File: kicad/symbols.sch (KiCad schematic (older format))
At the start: 13 parts

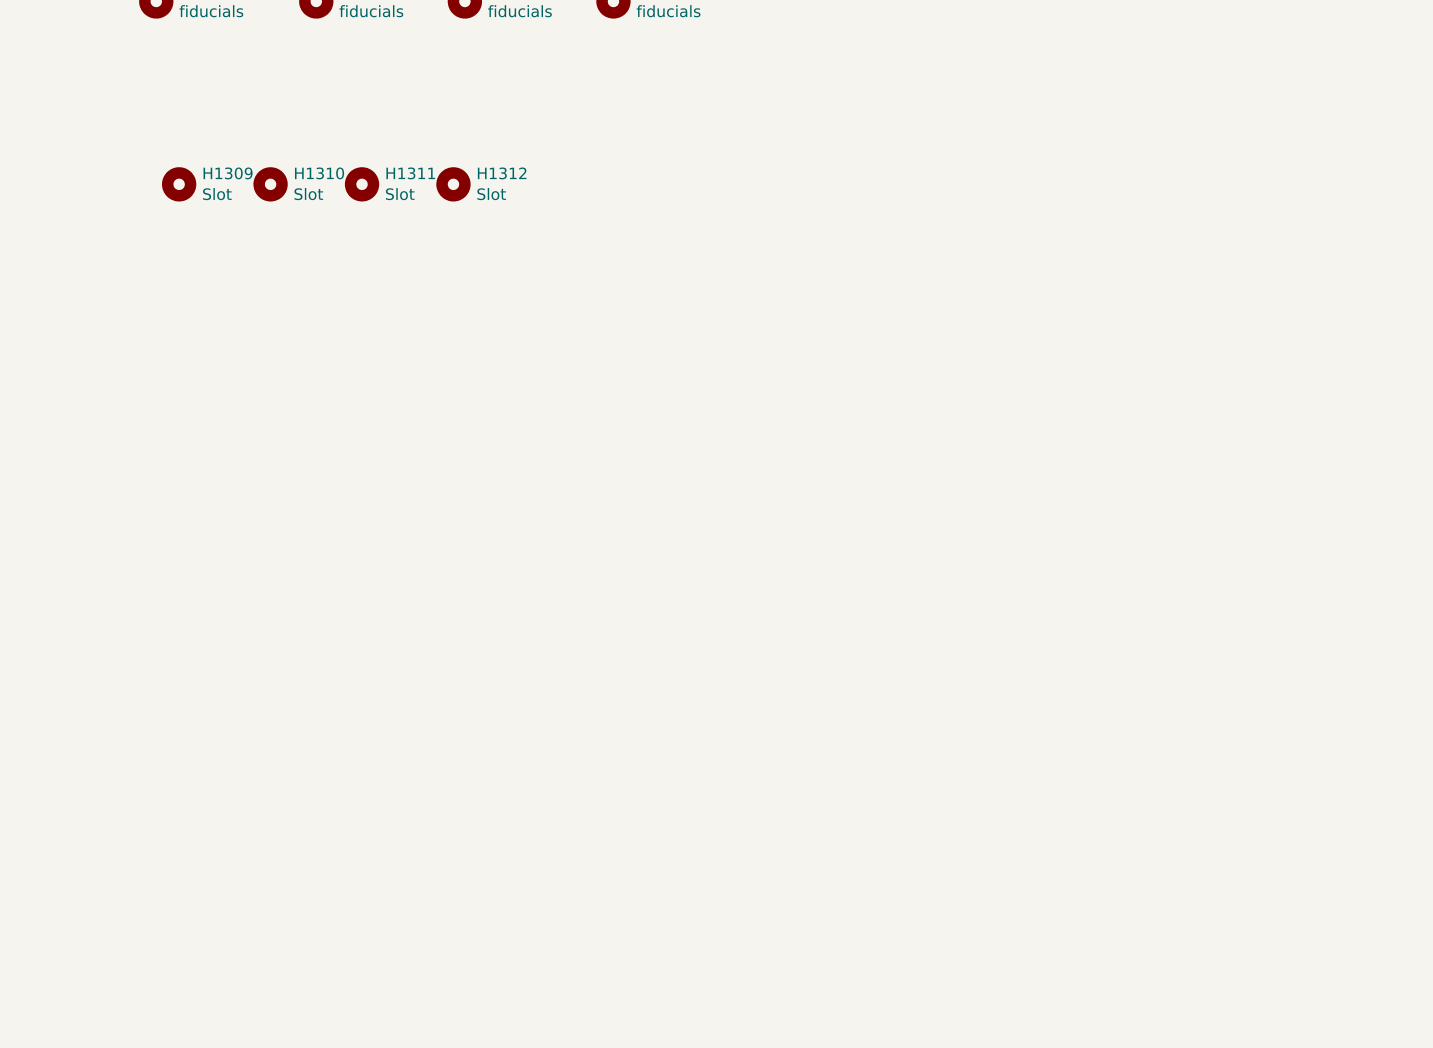
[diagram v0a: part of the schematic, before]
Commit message: added sloted holes everyware
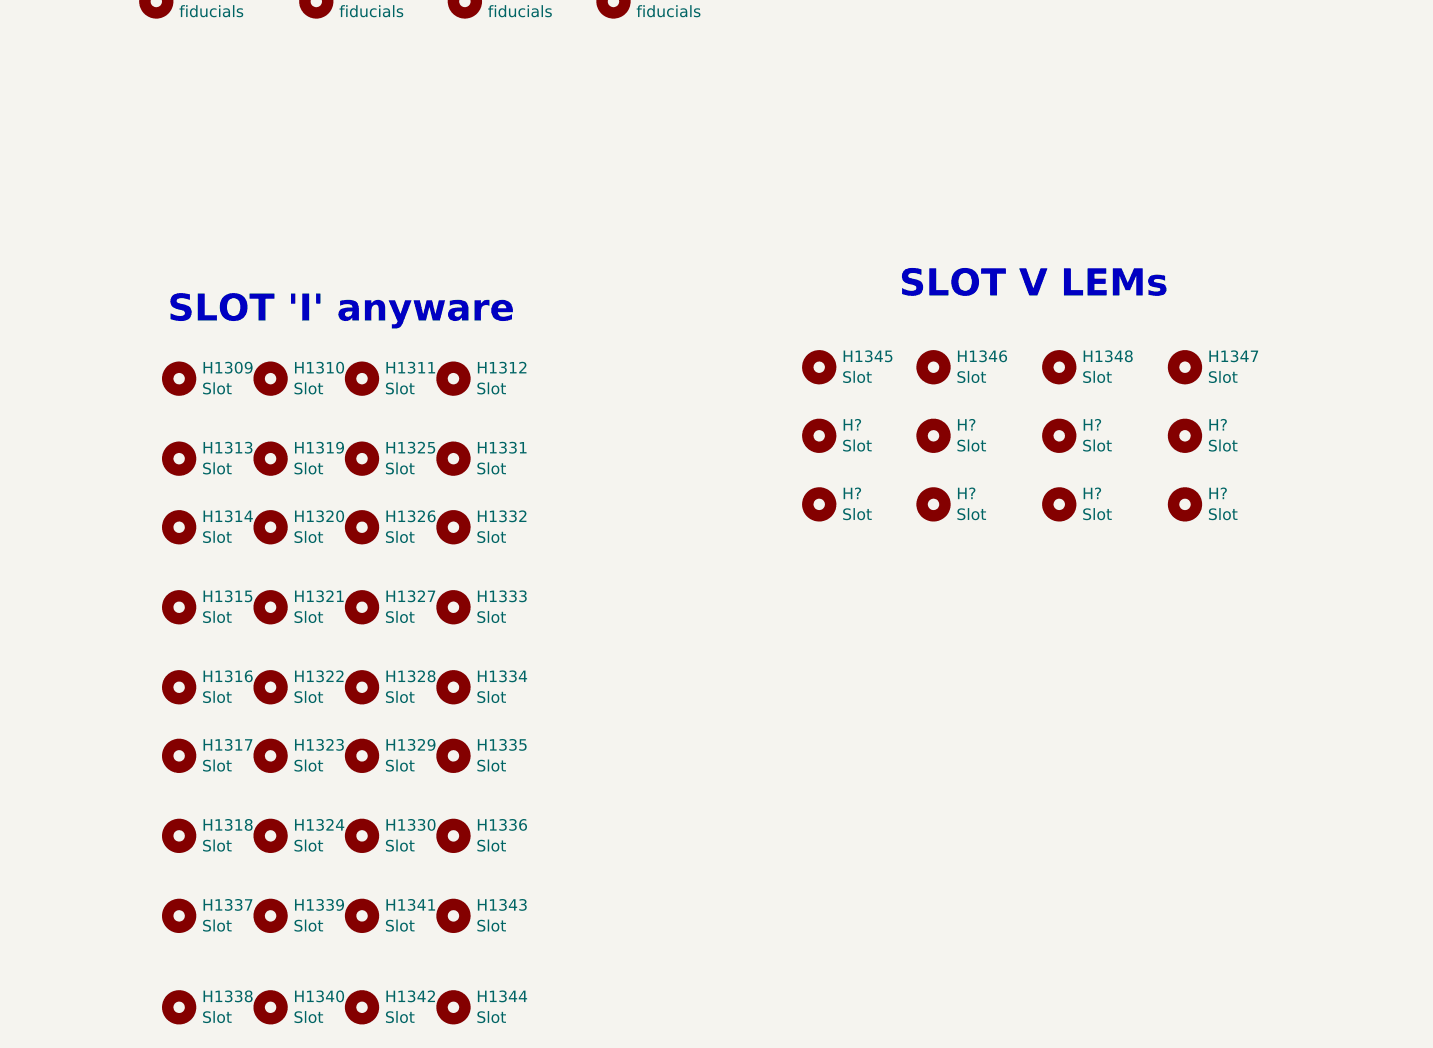
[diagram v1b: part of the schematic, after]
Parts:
- added H1313, H1314, H1315, H1316, H1317, H1318, H1319, H1320, H1321, H1322, H1323, H1324, H1325, H1326, H1327, H1328, H1329, H1330, H1331, H1332, H1333, H1334, H1335, H1336, H1337, H1338, H1339, H1340, H1341, H1342, H1343, H1344: Slot, servo:slot, symbol Mechanical:MountingHole
- added H1345, H1346, H1347, H1348, H? (x8): Slot, servo:slot_v, symbol Mechanical:MountingHole
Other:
- note added: "SLOT 'I' anyware\n\n\n"
- note added: "SLOT V LEMs\n\n"
- moved on the sheet: H1309, H1310, H1311, H1312

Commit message: save to rename IC'a
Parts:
- gave numbers to parts that had none: 8
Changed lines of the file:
@@
 $EndComp
 $Comp
-L Mechanical:MountingHole H?
+L Mechanical:MountingHole H1349
 U 1 1 5E41C227
 P 7050 4800
-F 0 "H?" H 7150 4846 50  0000 L CNN
+F 0 "H1349" H 7150 4846 50  0000 L CNN
 F 1 "Slot" H 7150 4755 50  0000 L CNN
 F 2 "servo:slot_v" H 7050 4800 50  0001 C CNN
@@
 $EndComp
 $Comp
-L Mechanical:MountingHole H?
+L Mechanical:MountingHole H1351
 U 1 1 5E41C22E
 P 7550 4800
-F 0 "H?" H 7650 4846 50  0000 L CNN
+F 0 "H1351" H 7650 4846 50  0000 L CNN
 F 1 "Slot" H 7650 4755 50  0000 L CNN
 F 2 "servo:slot_v" H 7550 4800 50  0001 C CNN
@@
 $EndComp
 $Comp
-L Mechanical:MountingHole H?
+L Mechanical:MountingHole H1355
 U 1 1 5E41C235
 P 8650 4800
-F 0 "H?" H 8750 4846 50  0000 L CNN
+F 0 "H1355" H 8750 4846 50  0000 L CNN
 F 1 "Slot" H 8750 4755 50  0000 L CNN
 F 2 "servo:slot_v" H 8650 4800 50  0001 C CNN
@@
 $EndComp
 $Comp
-L Mechanical:MountingHole H?
+L Mechanical:MountingHole H1353
 U 1 1 5E41C23C
 P 8100 4800
-F 0 "H?" H 8200 4846 50  0000 L CNN
+F 0 "H1353" H 8200 4846 50  0000 L CNN
 F 1 "Slot" H 8200 4755 50  0000 L CNN
 F 2 "servo:slot_v" H 8100 4800 50  0001 C CNN
@@
 $EndComp
 $Comp
-L Mechanical:MountingHole H?
+L Mechanical:MountingHole H1350
 U 1 1 5E41C3B7
 P 7050 5100
-F 0 "H?" H 7150 5146 50  0000 L CNN
+F 0 "H1350" H 7150 5146 50  0000 L CNN
 F 1 "Slot" H 7150 5055 50  0000 L CNN
 F 2 "servo:slot_v" H 7050 5100 50  0001 C CNN
@@
 $EndComp
 $Comp
-L Mechanical:MountingHole H?
+L Mechanical:MountingHole H1352
 U 1 1 5E41C3BE
 P 7550 5100
-F 0 "H?" H 7650 5146 50  0000 L CNN
+F 0 "H1352" H 7650 5146 50  0000 L CNN
 F 1 "Slot" H 7650 5055 50  0000 L CNN
 F 2 "servo:slot_v" H 7550 5100 50  0001 C CNN
@@
 $EndComp
 $Comp
-L Mechanical:MountingHole H?
+L Mechanical:MountingHole H1356
 U 1 1 5E41C3C5
 P 8650 5100
-F 0 "H?" H 8750 5146 50  0000 L CNN
+F 0 "H1356" H 8750 5146 50  0000 L CNN
 F 1 "Slot" H 8750 5055 50  0000 L CNN
 F 2 "servo:slot_v" H 8650 5100 50  0001 C CNN
@@
 $EndComp
 $Comp
-L Mechanical:MountingHole H?
+L Mechanical:MountingHole H1354
 U 1 1 5E41C3CC
 P 8100 5100
-F 0 "H?" H 8200 5146 50  0000 L CNN
+F 0 "H1354" H 8200 5146 50  0000 L CNN
 F 1 "Slot" H 8200 5055 50  0000 L CNN
 F 2 "servo:slot_v" H 8100 5100 50  0001 C CNN

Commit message: serigrafia...
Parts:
- added logo1301: nanocut, servo:logo_nanocut, symbol servo:logo
- added logo1302: pslavkin, servo:logo_pslavkin, symbol servo:logo
- added logo1303: recycler, Symbol:WEEE-Logo_5.6x8mm_SilkScreen, symbol servo:logo
- added ref1301: kicad, Symbol:KiCad-Logo_6mm_SilkScreen, symbol servo:logo
- added ref1302, ref1303, ref1304, ref1305: high_voltage, servo:Symbol_Highvoltage_Type1_CopperTop_Small, symbol servo:high_voltage
- H1309, H1310, H1311, H1312, H1313, H1314, H1315, H1316, H1317, H1318, H1319, H1320, H1321, H1322, H1323, H1324, H1325, H1326, H1327, H1328, H1329, H1330, H1331, H1332, H1333, H1334, H1335, H1336, H1337, H1338, H1339, H1340, H1341, H1342, H1343, H1344: footprint servo:slot -> servo:slot2

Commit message: serigraphi, improve of nets. change of soic 8 footprint
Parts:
- added H1357, H1358: Slot, servo:slot2, symbol Mechanical:MountingHole
- added H1359: Slot, MountingHole:MountingHole_3.2mm_M3_Pad_Via, symbol Mechanical:MountingHole
- added logo1304: servo_driver, servo:logo_pslavkin, symbol servo:logo
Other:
- note added: "mounting holes\n"
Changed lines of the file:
@@
 L servo:high_voltage ref1302
 U 1 1 5E38C9D6
-P 12250 3100
-F 0 "ref1302" V 12160 3100 50  0001 C CNN
-F 1 "high_voltage" V 12340 3100 50  0001 C CNN
-F 2 "servo:Symbol_Highvoltage_Type1_CopperTop_Small" H 12450 3600 50  0001 C CNN
-F 3 "~" H 12650 3000 50  0001 C CNN
-	1    12250 3100
+P 13200 3450
+F 0 "ref1302" V 13110 3450 50  0001 C CNN
+F 1 "high_voltage" V 13290 3450 50  0001 C CNN
+F 2 "servo:Symbol_Highvoltage_Type1_CopperTop_Small" H 13400 3950 50  0001 C CNN
+F 3 "~" H 13600 3350 50  0001 C CNN
+	1    13200 3450
 	1    0    0    -1
 $EndComp
@@
 L servo:high_voltage ref1303
 U 1 1 5E39D206
-P 12400 3100
-F 0 "ref1303" V 12310 3100 50  0001 C CNN
-F 1 "high_voltage" V 12490 3100 50  0001 C CNN
-F 2 "servo:Symbol_Highvoltage_Type1_CopperTop_Small" H 12600 3600 50  0001 C CNN
-F 3 "~" H 12800 3000 50  0001 C CNN
-	1    12400 3100
+P 13350 3450
+F 0 "ref1303" V 13260 3450 50  0001 C CNN
+F 1 "high_voltage" V 13440 3450 50  0001 C CNN
+F 2 "servo:Symbol_Highvoltage_Type1_CopperTop_Small" H 13550 3950 50  0001 C CNN
+F 3 "~" H 13750 3350 50  0001 C CNN
+	1    13350 3450
 	1    0    0    -1
 $EndComp
@@
 L servo:high_voltage ref1304
 U 1 1 5E39D283
-P 12550 3100
-F 0 "ref1304" V 12460 3100 50  0001 C CNN
-F 1 "high_voltage" V 12640 3100 50  0001 C CNN
-F 2 "servo:Symbol_Highvoltage_Type1_CopperTop_Small" H 12750 3600 50  0001 C CNN
-F 3 "~" H 12950 3000 50  0001 C CNN
-	1    12550 3100
+P 13500 3450
+F 0 "ref1304" V 13410 3450 50  0001 C CNN
+F 1 "high_voltage" V 13590 3450 50  0001 C CNN
+F 2 "servo:Symbol_Highvoltage_Type1_CopperTop_Small" H 13700 3950 50  0001 C CNN
+F 3 "~" H 13900 3350 50  0001 C CNN
+	1    13500 3450
 	1    0    0    -1
 $EndComp
@@
 L servo:high_voltage ref1305
 U 1 1 5E39D300
-P 12700 3100
-F 0 "ref1305" V 12610 3100 50  0001 C CNN
-F 1 "high_voltage" V 12790 3100 50  0001 C CNN
-F 2 "servo:Symbol_Highvoltage_Type1_CopperTop_Small" H 12900 3600 50  0001 C CNN
-F 3 "~" H 13100 3000 50  0001 C CNN
-	1    12700 3100
+P 13650 3450
+F 0 "ref1305" V 13560 3450 50  0001 C CNN
+F 1 "high_voltage" V 13740 3450 50  0001 C CNN
+F 2 "servo:Symbol_Highvoltage_Type1_CopperTop_Small" H 13850 3950 50  0001 C CNN
+F 3 "~" H 14050 3350 50  0001 C CNN
+	1    13650 3450
 	1    0    0    -1
 $EndComp
+$Comp
+L Mechanical:MountingHole H1357
+U 1 1 5E39587A
+P 5450 7600
+F 0 "H1357" H 5550 7646 50  0000 L CNN
+F 1 "Slot" H 5550 7555 50  0000 L CNN
+F 2 "servo:slot2" H 5450 7600 50  0001 C CNN
+F 3 "~" H 5450 7600 50  0001 C CNN
+	1    5450 7600
+	1    0    0    -1
+$EndComp
+$Comp
+L Mechanical:MountingHole H1358
+U 1 1 5E397C76
+P 5050 7600
+F 0 "H1358" H 5150 7646 50  0000 L CNN
+F 1 "Slot" H 5150 7555 50  0000 L CNN
+F 2 "servo:slot2" H 5050 7600 50  0001 C CNN
+F 3 "~" H 5050 7600 50  0001 C CNN
+	1    5050 7600
+	1    0    0    -1
+$EndComp
+$Comp
+L Mechanical:MountingHole H1359
+U 1 1 5E3A215E
+P 10250 4400
+F 0 "H1359" H 10350 4446 50  0000 L CNN
+F 1 "Slot" H 10350 4355 50  0000 L CNN
+F 2 "MountingHole:MountingHole_3.2mm_M3_Pad_Via" H 10250 4400 50  0001 C CNN
+F 3 "~" H 10250 4400 50  0001 C CNN
+	1    10250 4400
+	1    0    0    -1
+$EndComp
+Text Notes 9750 4100 0    118  ~ 24
+mounting holes\n
+$Comp
+L servo:logo logo1304
+U 1 1 5E3A5304
+P 13350 3900
+F 0 "logo1304" H 13350 4100 50  0001 C CNN
+F 1 "servo_driver" H 13678 3900 50  0000 L CNN
+F 2 "servo:logo_pslavkin" H 13350 3900 50  0001 C CNN
+F 3 "~" H 13350 3900 50  0001 C CNN
+	1    13350 3900
+	1    0    0    -1
+$EndComp

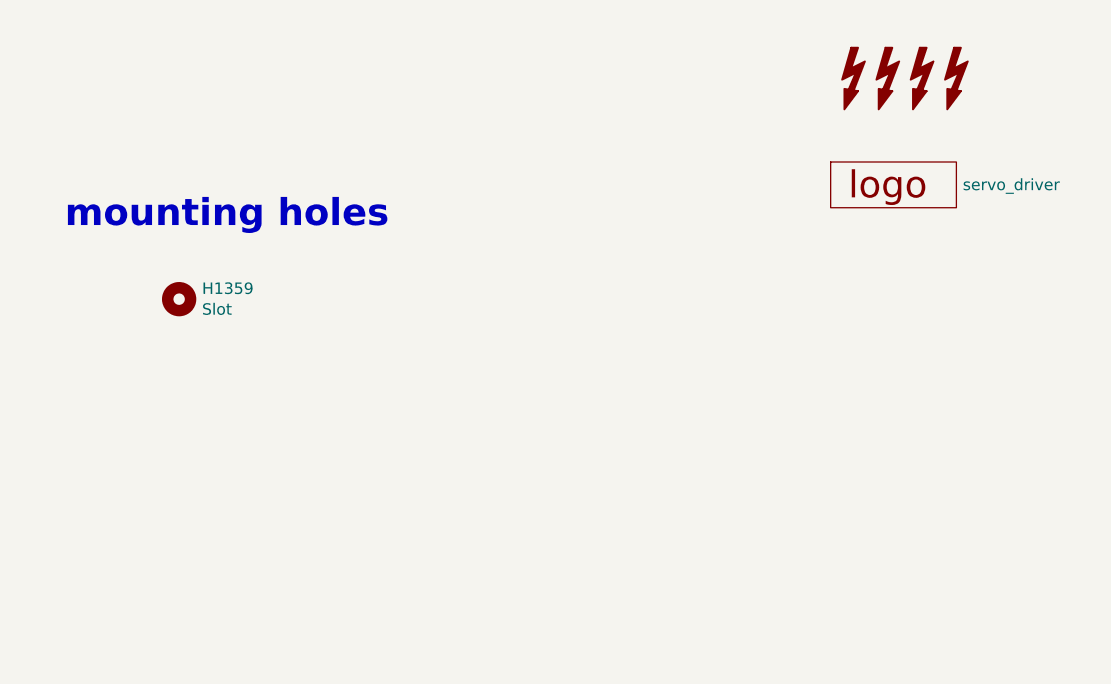
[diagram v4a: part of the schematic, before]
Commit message: more serigraphy and now begin with planes
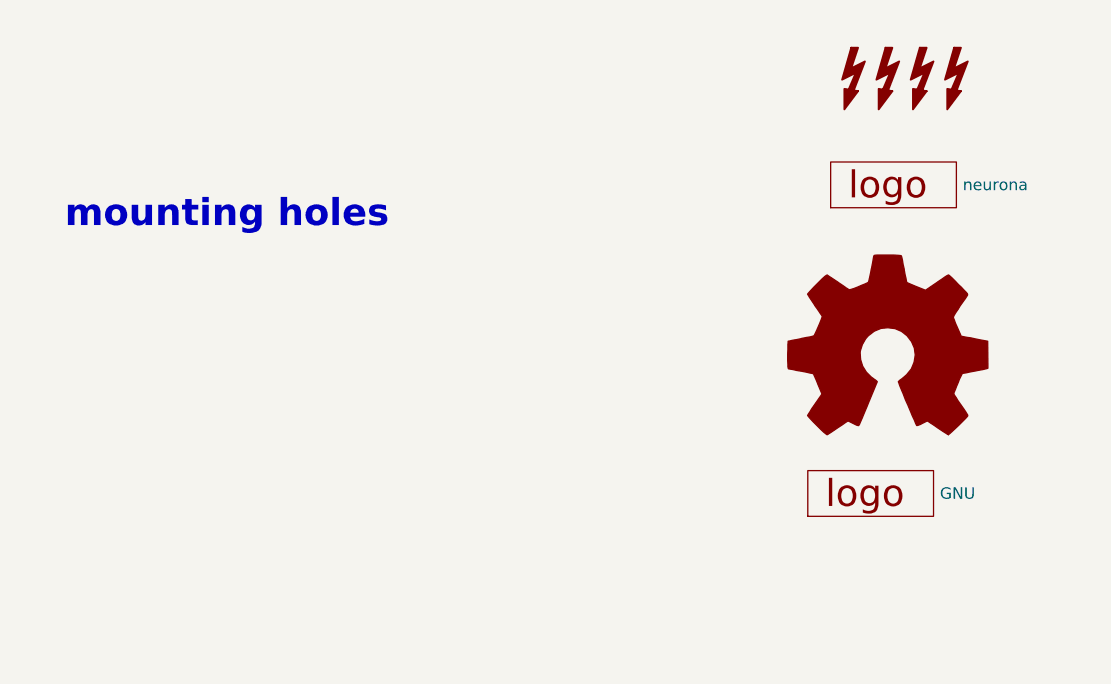
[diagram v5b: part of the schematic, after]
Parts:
- removed H1359: Slot, MountingHole:MountingHole_3.2mm_M3_Pad_Via, symbol Mechanical:MountingHole
- added LOGO1301: Logo_Open_Hardware_Large, Symbol:OSHW-Symbol_13.4x12mm_SilkScreen, symbol Graphic:Logo_Open_Hardware_Large
- added logo1305: neurona, servo:logo_neurona_20mm, symbol servo:logo
- logo1304: value servo_driver -> GNU; footprint servo:logo_pslavkin -> Symbol:Symbol_GNU-Logo_SilkscreenTop
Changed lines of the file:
@@
-	1    0    0    -1
-$EndComp
-$Comp
-L Mechanical:MountingHole H1359
-U 1 1 5E3A215E
-P 10250 4400
-F 0 "H1359" H 10350 4446 50  0000 L CNN
-F 1 "Slot" H 10350 4355 50  0000 L CNN
-F 2 "MountingHole:MountingHole_3.2mm_M3_Pad_Via" H 10250 4400 50  0001 C CNN
-F 3 "~" H 10250 4400 50  0001 C CNN
-	1    10250 4400
 	1    0    0    -1
 $EndComp
@@
 mounting holes\n
 $Comp
-L servo:logo logo1304
-U 1 1 5E3A5304
+L servo:logo logo1305
+U 1 1 5E3B996A
 P 13350 3900
-F 0 "logo1304" H 13350 4100 50  0001 C CNN
-F 1 "servo_driver" H 13678 3900 50  0000 L CNN
-F 2 "servo:logo_pslavkin" H 13350 3900 50  0001 C CNN
+F 0 "logo1305" H 13350 4100 50  0001 C CNN
+F 1 "neurona" H 13678 3900 50  0000 L CNN
+F 2 "servo:logo_neurona_20mm" H 13350 3900 50  0001 C CNN
 F 3 "~" H 13350 3900 50  0001 C CNN
 	1    13350 3900
+	1    0    0    1
+$EndComp
+$Comp
+L Graphic:Logo_Open_Hardware_Large LOGO1301
+U 1 1 5E3C6A52
+P 13350 4650
+F 0 "LOGO1301" H 13350 5150 50  0001 C CNN
+F 1 "Logo_Open_Hardware_Large" H 13350 4250 50  0001 C CNN
+F 2 "Symbol:OSHW-Symbol_13.4x12mm_SilkScreen" H 13350 4650 50  0001 C CNN
+F 3 "~" H 13350 4650 50  0001 C CNN
+	1    13350 4650
 	1    0    0    -1
 $EndComp
+$Comp
+L servo:logo logo1304
+U 1 1 5E3C6E44
+P 13250 5250
+F 0 "logo1304" H 13250 5450 50  0001 C CNN
+F 1 "GNU" H 13578 5250 50  0000 L CNN
+F 2 "Symbol:Symbol_GNU-Logo_SilkscreenTop" H 13250 5250 50  0001 C CNN
+F 3 "~" H 13250 5250 50  0001 C CNN
+	1    13250 5250
+	1    0    0    1
+$EndComp
 $EndSCHEMATC

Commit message: improving tracks under uC
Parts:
- H1301, H1303, H1305, H1307: footprint Fiducial:Fiducial_1mm_Dia_2.54mm_Outer_CopperTop -> servo:Fiducial_1mm_Dia_2.54mm_Outer_CopperTop
- H1302, H1304, H1306, H1308: footprint Fiducial:Fiducial_1mm_Dia_2.54mm_Outer_CopperBottom -> servo:Fiducial_1mm_Dia_2.54mm_Outer_CopperBottom
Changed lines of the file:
@@
 F 0 "H1301" H 4200 2046 50  0000 L CNN
 F 1 "fiducials" H 4200 1955 50  0000 L CNN
-F 2 "Fiducial:Fiducial_1mm_Dia_2.54mm_Outer_CopperTop" H 4100 2000 50  0001 C CNN
+F 2 "servo:Fiducial_1mm_Dia_2.54mm_Outer_CopperTop" H 4100 2000 50  0001 C CNN
 F 3 "~" H 4100 2000 50  0001 C CNN
 	1    4100 2000
@@
 F 0 "H1302" H 4250 2946 50  0000 L CNN
 F 1 "fiducials" H 4250 2855 50  0000 L CNN
-F 2 "Fiducial:Fiducial_1mm_Dia_2.54mm_Outer_CopperBottom" H 4150 2900 50  0001 C CNN
+F 2 "servo:Fiducial_1mm_Dia_2.54mm_Outer_CopperBottom" H 4150 2900 50  0001 C CNN
 F 3 "~" H 4150 2900 50  0001 C CNN
 	1    4150 2900
@@
 F 0 "H1303" H 4900 2046 50  0000 L CNN
 F 1 "fiducials" H 4900 1955 50  0000 L CNN
-F 2 "Fiducial:Fiducial_1mm_Dia_2.54mm_Outer_CopperTop" H 4800 2000 50  0001 C CNN
+F 2 "servo:Fiducial_1mm_Dia_2.54mm_Outer_CopperTop" H 4800 2000 50  0001 C CNN
 F 3 "~" H 4800 2000 50  0001 C CNN
 	1    4800 2000
@@
 F 0 "H1305" H 5550 2046 50  0000 L CNN
 F 1 "fiducials" H 5550 1955 50  0000 L CNN
-F 2 "Fiducial:Fiducial_1mm_Dia_2.54mm_Outer_CopperTop" H 5450 2000 50  0001 C CNN
+F 2 "servo:Fiducial_1mm_Dia_2.54mm_Outer_CopperTop" H 5450 2000 50  0001 C CNN
 F 3 "~" H 5450 2000 50  0001 C CNN
 	1    5450 2000
@@
 F 0 "H1307" H 6250 2046 50  0000 L CNN
 F 1 "fiducials" H 6250 1955 50  0000 L CNN
-F 2 "Fiducial:Fiducial_1mm_Dia_2.54mm_Outer_CopperTop" H 6150 2000 50  0001 C CNN
+F 2 "servo:Fiducial_1mm_Dia_2.54mm_Outer_CopperTop" H 6150 2000 50  0001 C CNN
 F 3 "~" H 6150 2000 50  0001 C CNN
 	1    6150 2000
@@
 F 0 "H1304" H 4950 2946 50  0000 L CNN
 F 1 "fiducials" H 4950 2855 50  0000 L CNN
-F 2 "Fiducial:Fiducial_1mm_Dia_2.54mm_Outer_CopperBottom" H 4850 2900 50  0001 C CNN
+F 2 "servo:Fiducial_1mm_Dia_2.54mm_Outer_CopperBottom" H 4850 2900 50  0001 C CNN
 F 3 "~" H 4850 2900 50  0001 C CNN
 	1    4850 2900
@@
 F 0 "H1306" H 5600 2946 50  0000 L CNN
 F 1 "fiducials" H 5600 2855 50  0000 L CNN
-F 2 "Fiducial:Fiducial_1mm_Dia_2.54mm_Outer_CopperBottom" H 5500 2900 50  0001 C CNN
+F 2 "servo:Fiducial_1mm_Dia_2.54mm_Outer_CopperBottom" H 5500 2900 50  0001 C CNN
 F 3 "~" H 5500 2900 50  0001 C CNN
 	1    5500 2900
@@
 F 0 "H1308" H 6250 2946 50  0000 L CNN
 F 1 "fiducials" H 6250 2855 50  0000 L CNN
-F 2 "Fiducial:Fiducial_1mm_Dia_2.54mm_Outer_CopperBottom" H 6150 2900 50  0001 C CNN
+F 2 "servo:Fiducial_1mm_Dia_2.54mm_Outer_CopperBottom" H 6150 2900 50  0001 C CNN
 F 3 "~" H 6150 2900 50  0001 C CNN
 	1    6150 2900
